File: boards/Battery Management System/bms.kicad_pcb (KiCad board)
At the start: 2 copper layers, 28 parts, among them J2 1986660-2, J3 B5B-XH-A, U1 BD48L32G, U2 BD48L32G, U3 BD48L32G, U4 BD48L32G, U5 SN74HC08DR

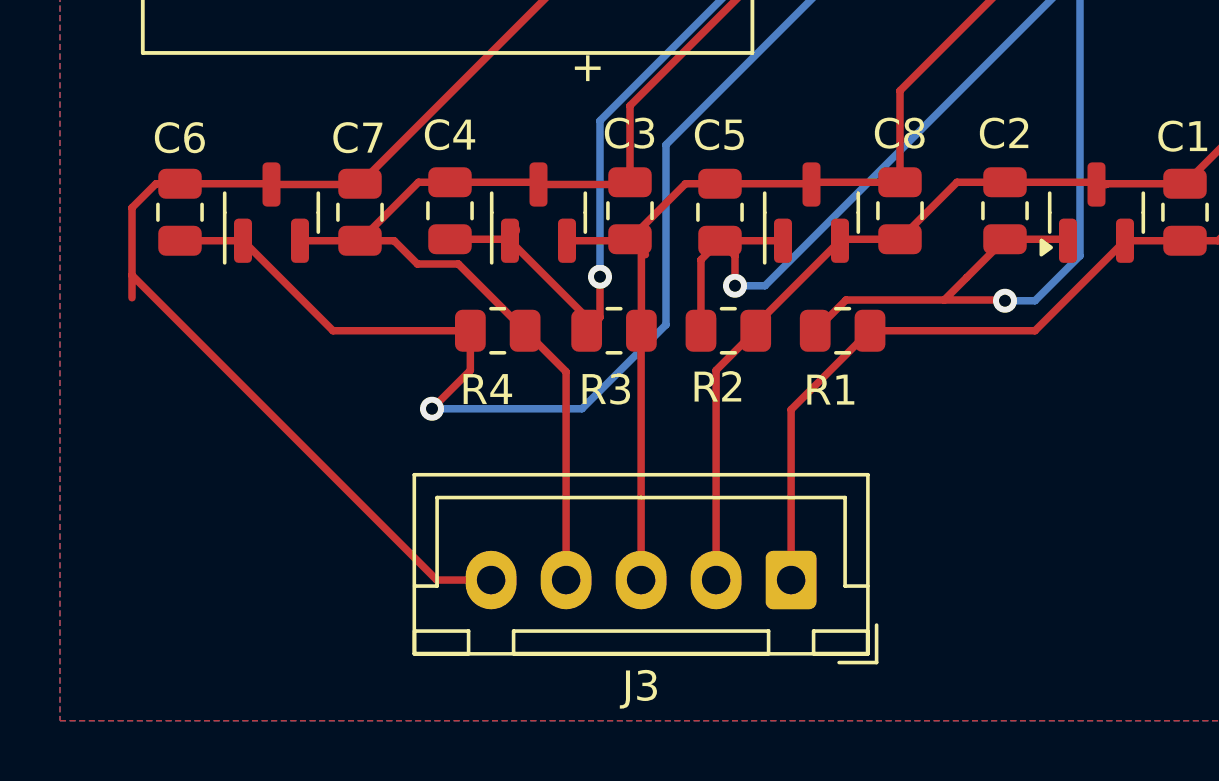
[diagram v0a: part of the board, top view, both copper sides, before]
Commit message: Flipped J3 terminal block on BMS
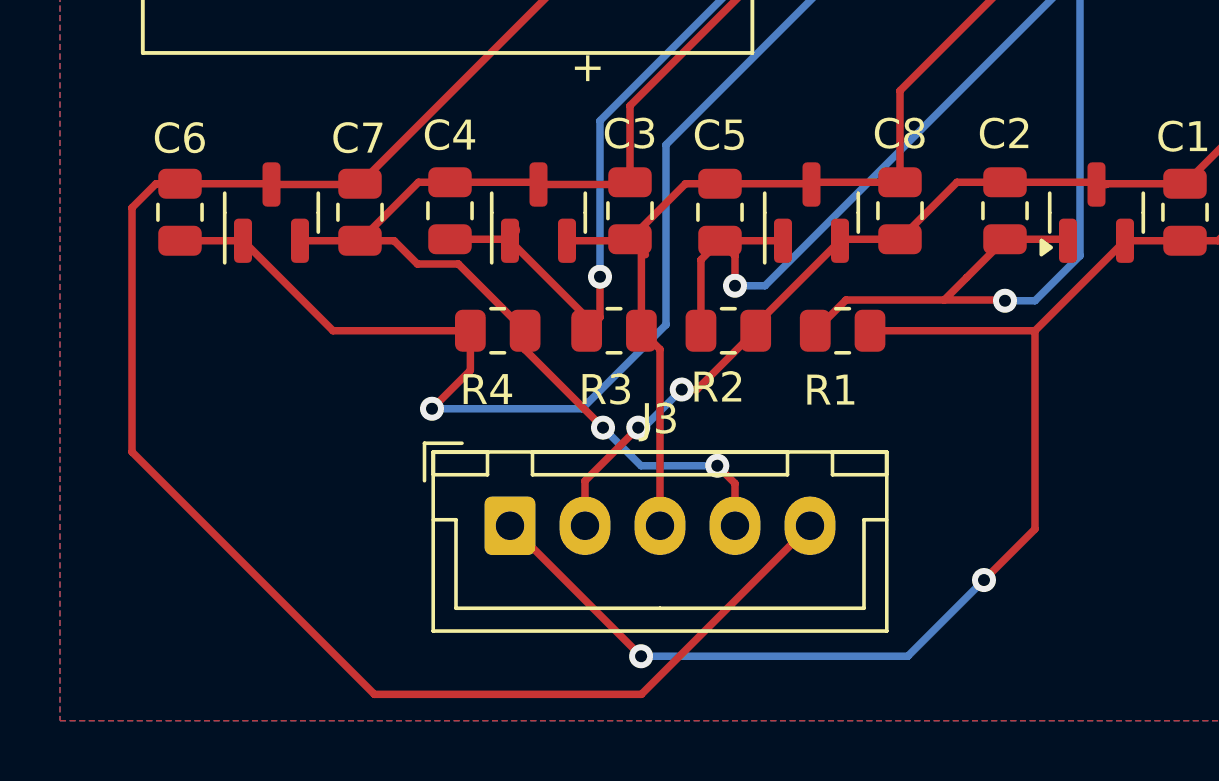
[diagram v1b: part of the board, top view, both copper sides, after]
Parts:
- moved J3 9.54 mm to (35.0, 65.5), turned to 0 degrees
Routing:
- net /V_CELL_1: track 48.7 -> 66.9 mm, vias 2 -> 4
- net GND: track 63.3 -> 80.5 mm
- net /V_CELL_4: track 60.8 -> 62.8 mm, vias 0 -> 2
- net /V_CELL_3: track 53.3 -> 52.5 mm
- net /V_CELL_2: track 84.8 -> 85.2 mm, vias 0 -> 2
